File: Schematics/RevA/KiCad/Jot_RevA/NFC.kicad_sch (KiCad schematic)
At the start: 3 parts

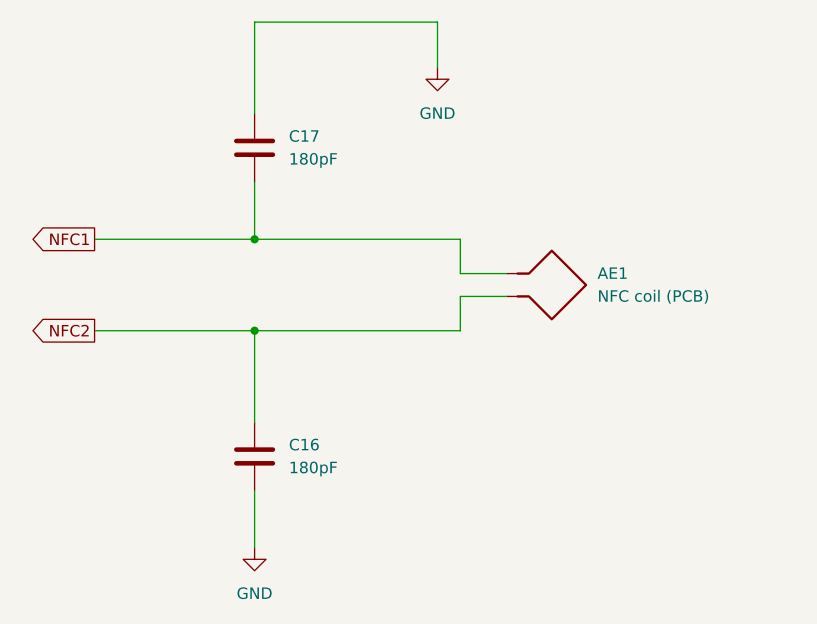
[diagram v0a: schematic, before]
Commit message: Rev A layout: board outline, mounting holes, all parts placed
- 37 x 60 mm 4-layer, 1.0 mm board, 3 mm corners, USB tab to Y 132.6 so the
  HRO socket face sits about 0.9 mm behind the case surface
- H1-H4 M2 holes at the case standoff positions
- Case-fixed parts locked: J1, U1 (antenna at the top edge), SW1, D1-D3
- NFC: external Molex 146236-0101 flex antenna on AE1 solder-wire holes,
  C16/C17 82 pF (Nordic PS p461 tuning for 3.1 uH), C18/C19 spare tuning
  caps (DNP)
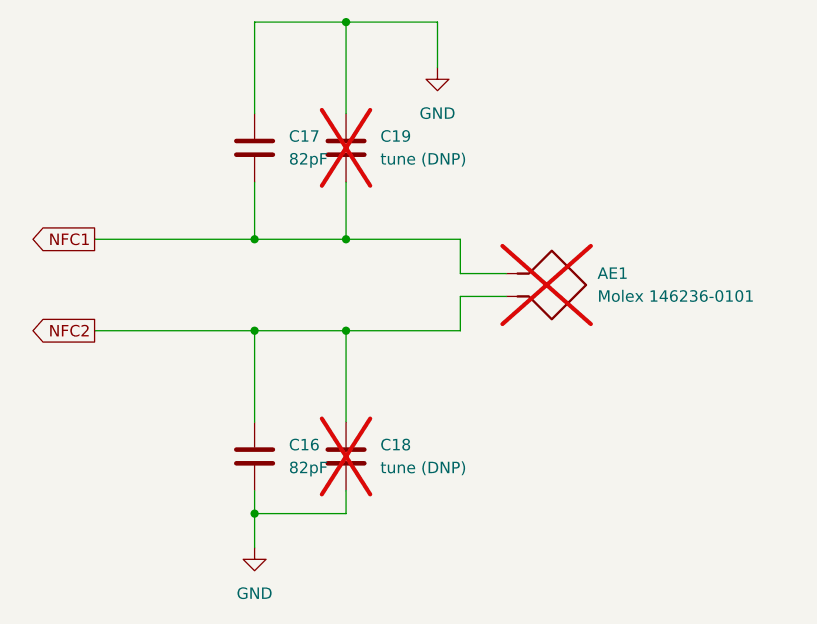
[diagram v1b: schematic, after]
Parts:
- added C18, C19: tune (DNP), Capacitor_SMD:C_0402_1005Metric, symbol Device:C
- AE1: value NFC coil (PCB) -> Molex 146236-0101; footprint (none) -> Connector_Wire:SolderWire-0.1sqmm_1x02_P3.6mm_D0.4mm_OD1mm; now not fitted; now left out of the parts list
- C16, C17: value 180pF -> 82pF
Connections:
- net GND: now also C18.2, C19.1
- net NFC1: now also C19.2
- net NFC2: now also C18.1
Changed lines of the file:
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@@
 			)
 		)
-		(property "Value" "180pF"
+		(property "Value" "82pF"
 			(at 151.13 111.7599 0)
 			(show_name no)
@@
 		(body_style 1)
 		(exclude_from_sim no)
-		(in_bom yes)
+		(in_bom no)
 		(on_board yes)
-		(in_pos_files yes)
-		(dnp no)
+		(in_pos_files no)
+		(dnp yes)
 		(fields_autoplaced yes)
 		(property "Reference" "AE1"
@@
 			)
 		)
-		(property "Value" "NFC coil (PCB)"
+		(property "Value" "Molex 146236-0101"
 			(at 185.42 92.7099 90)
 			(show_name no)
@@
 			)
 		)
-		(property "Footprint" ""
+		(property "Footprint" "Connector_Wire:SolderWire-0.1sqmm_1x02_P3.6mm_D0.4mm_OD1mm"
 			(at 180.34 90.17 0)
 			(hide yes)
@@
 			)
 		)
-		(property "Value" "180pF"
+		(property "Value" "82pF"
 			(at 151.13 77.4699 0)
 			(show_name no)
@@
 		)
 	)
+	(symbol
+		(lib_id "Device:C")
+		(at 157.48 76.2 0)
+		(unit 1)
+		(body_style 1)
+		(exclude_from_sim no)
+		(in_bom no)
+		(on_board yes)
+		(in_pos_files no)
+		(dnp yes)
+		(fields_autoplaced yes)
+		(property "Reference" "C19"
+			(at 161.29 74.9299 0)
+			(show_name no)
+			(do_not_autoplace no)
+			(effects
+				(font
+					(size 1.27 1.27)
+				)
+				(justify left)
+			)
+		)
+		(property "Value" "tune (DNP)"
+			(at 161.29 77.4699 0)
+			(show_name no)
+			(do_not_autoplace no)
+			(effects
+				(font
+					(size 1.27 1.27)
+				)
+				(justify left)
+			)
+		)
+		(property "Footprint" "Capacitor_SMD:C_0402_1005Metric"
+			(at 158.4452 80.01 0)
+			(hide yes)
+			(show_name no)
+			(do_not_autoplace no)
+			(effects
+				(font
+					(size 1.27 1.27)
+				)
+			)
+		)
+		(property "Datasheet" ""
+			(at 157.48 76.2 0)
+			(hide yes)
+			(show_name no)
+			(do_not_autoplace no)
+			(effects
+				(font
+					(size 1.27 1.27)
+				)
+			)
+		)
+		(property "Description" "Spare NFC tuning capacitor, fitted by hand only if needed"
+			(at 157.48 76.2 0)
+			(hide yes)
+			(show_name no)
+			(do_not_autoplace no)
+			(effects
+				(font
+					(size 1.27 1.27)
+				)
+			)
+		)
+		(pin "1"
+		)
+		(pin "2"
+		)
+		(instances
+			(project "Jot_RevA"
+				(path "/61747270-9f90-47b6-9c50-5ea1f41f259a/56e09d94-fc61-43ee-b4b8-8470d6a2f030"
+					(reference "C19")
+					(unit 1)
+				)
+			)
+		)
+	)
+	(symbol
+		(lib_id "Device:C")
+		(at 157.48 110.49 0)
+		(unit 1)
+		(body_style 1)
+		(exclude_from_sim no)
+		(in_bom no)
+		(on_board yes)
+		(in_pos_files no)
+		(dnp yes)
+		(fields_autoplaced yes)
+		(property "Reference" "C18"
+			(at 161.29 109.2199 0)
+			(show_name no)
+			(do_not_autoplace no)
+			(effects
+				(font
+					(size 1.27 1.27)
+				)
+				(justify left)
+			)
+		)
+		(property "Value" "tune (DNP)"
+			(at 161.29 111.7599 0)
+			(show_name no)
+			(do_not_autoplace no)
+			(effects
+				(font
+					(size 1.27 1.27)
+				)
+				(justify left)
+			)
+		)
+		(property "Footprint" "Capacitor_SMD:C_0402_1005Metric"
+			(at 158.4452 114.30 0)
+			(hide yes)
+			(show_name no)
+			(do_not_autoplace no)
+			(effects
+				(font
+					(size 1.27 1.27)
+				)
+			)
+		)
+		(property "Datasheet" ""
+			(at 157.48 110.49 0)
+			(hide yes)
+			(show_name no)
+			(do_not_autoplace no)
+			(effects
+				(font
+					(size 1.27 1.27)
+				)
+			)
+		)
+		(property "Description" "Spare NFC tuning capacitor, fitted by hand only if needed"
+			(at 157.48 110.49 0)
+			(hide yes)
+			(show_name no)
+			(do_not_autoplace no)
+			(effects
+				(font
+					(size 1.27 1.27)
+				)
+			)
+		)
+		(pin "1"
+		)
+		(pin "2"
+		)
+		(instances
+			(project "Jot_RevA"
+				(path "/61747270-9f90-47b6-9c50-5ea1f41f259a/56e09d94-fc61-43ee-b4b8-8470d6a2f030"
+					(reference "C18")
+					(unit 1)
+				)
+			)
+		)
+	)
+	(wire
+		(pts
+			(xy 157.48 72.39) (xy 157.48 62.23)
+		)
+		(stroke
+			(width 0)
+			(type default)
+		)
+	)
+	(wire
+		(pts
+			(xy 157.48 80.01) (xy 157.48 86.36)
+		)
+		(stroke
+			(width 0)
+			(type default)
+		)
+	)
+	(wire
+		(pts
+			(xy 157.48 106.68) (xy 157.48 96.52)
+		)
+		(stroke
+			(width 0)
+			(type default)
+		)
+	)
+	(wire
+		(pts
+			(xy 157.48 114.3) (xy 157.48 116.84)
+		)
+		(stroke
+			(width 0)
+			(type default)
+		)
+	)
+	(wire
+		(pts
+			(xy 157.48 116.84) (xy 147.32 116.84)
+		)
+		(stroke
+			(width 0)
+			(type default)
+		)
+	)
+	(junction
+		(at 157.48 62.23)
+		(diameter 0)
+		(color 0 0 0 0)
+	)
+	(junction
+		(at 157.48 86.36)
+		(diameter 0)
+		(color 0 0 0 0)
+	)
+	(junction
+		(at 157.48 96.52)
+		(diameter 0)
+		(color 0 0 0 0)
+	)
+	(junction
+		(at 147.32 116.84)
+		(diameter 0)
+		(color 0 0 0 0)
+	)
 )
